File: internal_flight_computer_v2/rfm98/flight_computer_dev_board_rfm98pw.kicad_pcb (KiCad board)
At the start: 4 copper layers, 88 x 94.5 mm, 102 parts, among them IC1 RP2040_QFN56, IC2 AZ1117CH-3.3TRG1, J1 Conn_ARM_JTAG_SWD_10, J10 BM04B-SRSS-TB(LF)(SN), J11 BM04B-SRSS-TB(LF)(SN), J12 BM04B-SRSS-TB(LF)(SN), J13 Breakout, J14 Battery, J15 Breakout, J2 FC to EPS Connector, J3 Life Makes Lemonade, J4 104031-0811, J5 BM04B-SRSS-TB(LF)(SN), J6 Conn_Coaxial, J7 Breakout, J8 USB_B_Micro, J9 BM04B-SRSS-TB(LF)(SN), SW1 KMR2, SW2 KMR2, U10 AP3602AKTR-G1, U3 MAX706RESA, U4 RFM98PW, U5 RFM9xBreakout, U6 W25Q128JV, U7 LSM6DSOTR, U8 LSM303AGRTR, U9 MCP25625-E/ML, Y1 12MHZ, Y3 16MHZ 12 pf

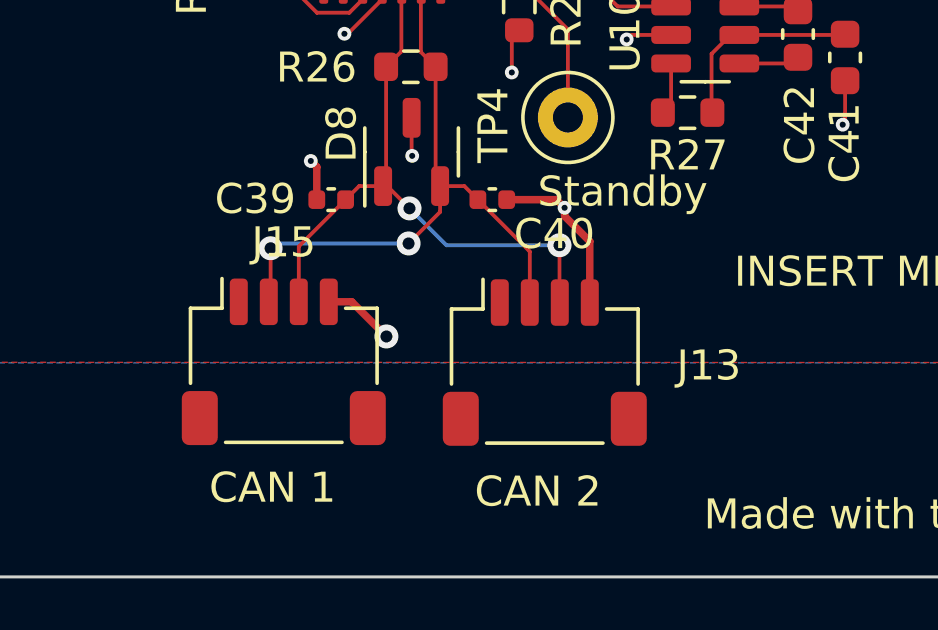
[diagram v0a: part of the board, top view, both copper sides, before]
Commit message: Huge Restructure of Dev Boards
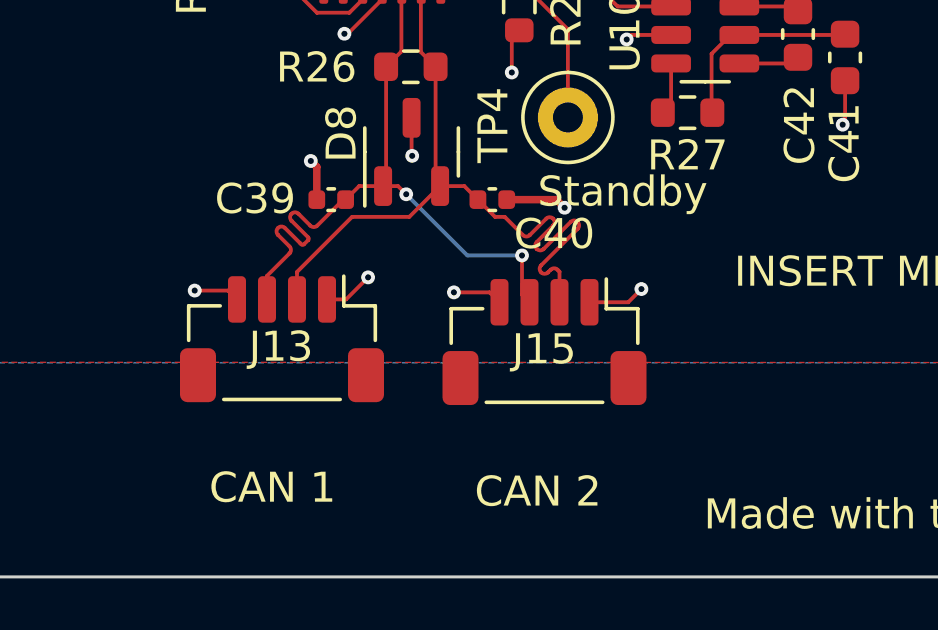
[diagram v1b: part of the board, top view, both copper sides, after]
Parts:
- J13, J15: footprint Connector_JST:JST_SH_SM04B-SRSS-TB_1x04-1MP_P1.00mm_Horizontal -> Connector_JST:JST_SH_BM04B-SRSS-TB_1x04-1MP_P1.00mm_Vertical
- moved J13 8.79 mm to (161.4, 134.2), turned to 180 degrees
- moved J15 8.72 mm to (170.1, 134.2), turned to 180 degrees
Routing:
- net CANH: track 21.1 -> 25.3 mm, vias 2 -> 0
- net 3.3V: track 60.6 -> 64.2 mm, vias 15 -> 17
- net GND: track 251.2 -> 248.5 mm, vias 73 -> 74
- net CANL: track 20.8 -> 23.1 mm

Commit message: Big Update of In Dev Boards
Mid Term update for all the boards being developed for use by the Irvington Team on Pleiades - Orpheus
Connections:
- D4 pad 1: /USBBOOT -> D3
- IC1 pad 15: ENAB_RF / D3 -> ENAB_RF / D2
- IC1 pad 16: /USBBOOT -> D3
- IC1 pad 17: VBUS_RESET / PC -> VBUS_RESET / D4
- IC1 pad 18: BURN_RELAY_A / VS -> BURN_RELAY_A / D5
- IC1 pad 27: D4 -> D6
- IC1 pad 28: D5 -> D7
- IC1 pad 29: D6 -> D8
- IC1 pad 30: D8 -> D9
- IC1 pad 39: D9 -> Neo_pwr
- IC1 pad 8: ENABLE_BURN / D7 -> ENABLE_BURN / PC
- IC1 pad 9: I2C_RESET / D2 -> I2C_RESET / VS
- J2 pad 2: BURN_RELAY_A / VS -> I2C_RESET / VS
- J2 pad 3: VBUS_RESET / PC -> ENABLE_BURN / PC
- J2 pad 4: I2C_RESET / D2 -> ENAB_RF / D2
- J2 pad 5: ENAB_RF / D3 -> D3
- J2 pad 9: ENABLE_BURN / D7 -> D7
- JP4 pad 3: D4 -> VBUS_RESET / D4
- JP9 pad 3: D5 -> BURN_RELAY_A / D5
- LED1 pad 1: 3v3 Spec -> Neo_pwr
- SW1 pad A: /USBBOOT -> D3
- SW1 pad A': /USBBOOT -> D3
- TP1 pad 1: /USBBOOT -> D3
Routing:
- net D3: track 0.00 -> 79.1 mm, vias 0 -> 3
- net I2C_RESET / VS: track 0.00 -> 54.0 mm, vias 0 -> 2
- net I2C_RESET / D2: track 51.6 -> 0.00 mm, vias 2 -> 0
- net ENABLE_BURN / PC: track 0.00 -> 48.7 mm, vias 0 -> 2
- net BURN_RELAY_A / VS: track 47.2 -> 0.00 mm, vias 2 -> 0
- net ENAB_RF / D2: track 0.00 -> 45.8 mm, vias 0 -> 2
- net VBUS_RESET / PC: track 44.2 -> 0.00 mm, vias 2 -> 0
- net ENAB_RF / D3: track 42.0 -> 0.00 mm, vias 2 -> 0
- net ENABLE_BURN / D7: track 41.3 -> 0.00 mm, vias 2 -> 0
- net VBUS_RESET / D4: track 0.00 -> 39.2 mm, vias 0 -> 2
- net D4: track 38.7 -> 0.00 mm, vias 3 -> 0
- net D5: track 38.2 -> 0.00 mm, vias 4 -> 0
- net BURN_RELAY_A / D5: track 0.00 -> 37.2 mm, vias 0 -> 2
- net /USBBOOT: track 34.9 -> 0.00 mm, vias 1 -> 0
- net D7: track 0.00 -> 30.9 mm, vias 0 -> 3
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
